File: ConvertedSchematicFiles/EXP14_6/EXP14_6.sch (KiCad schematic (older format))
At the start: 7 parts, among them U1 74393, U2 7448

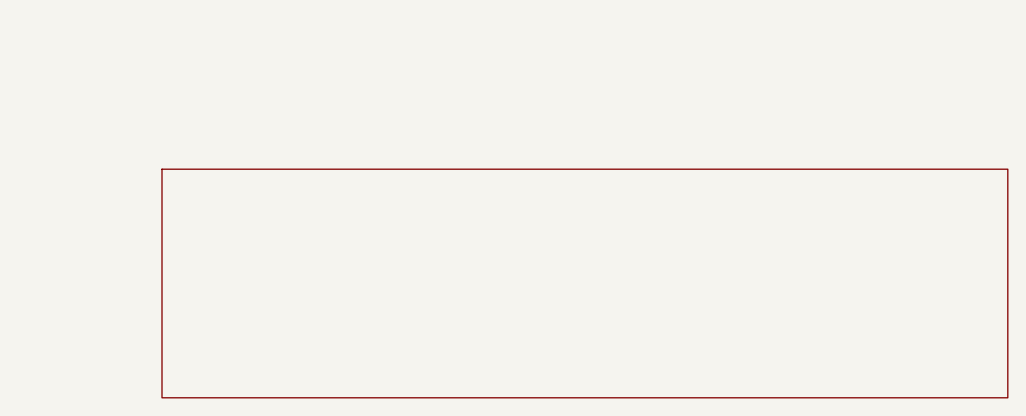
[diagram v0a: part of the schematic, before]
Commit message: Excluded some components. These no longer appear after conversion. When calling shell commands, filenames are in "quotes"
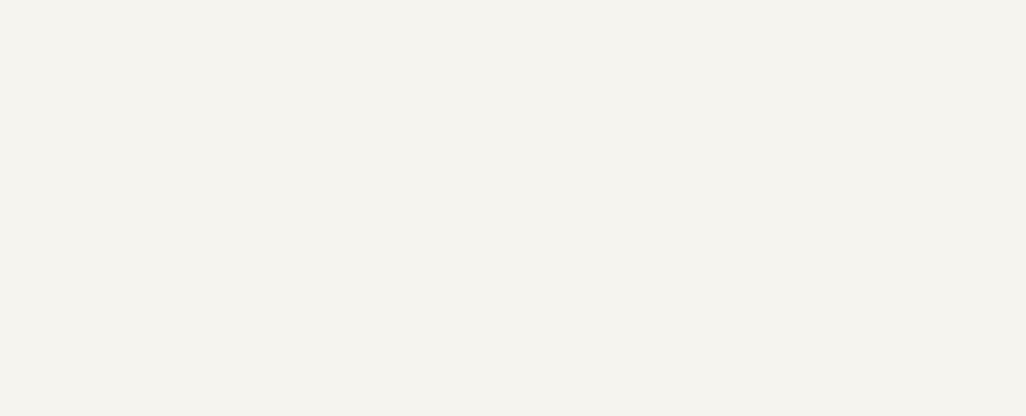
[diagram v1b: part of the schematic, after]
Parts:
- removed titleblk: titleblk, symbol TITLEBLK_PSPICE
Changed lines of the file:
@@
-	1    0    0    1
-$EndComp
-$Comp
-L TITLEBLK_PSPICE titleblk
-U 1 1 99885386
-P 9700 7200
-F 0 "titleblk" H 19400 14400 30  0001 L CNN
-F 1 "titleblk" H 19400 14480 30  0001 L CNN
-	1    9700 7200
 	1    0    0    1
 $EndComp

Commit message: Ports issue fixed. Now annotation for ports is #PWR? function added "itos"
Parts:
- removed +5V: +5V, symbol +5V_PSPICE
- removed EGND (x2): EGND, symbol EGND_PSPICE
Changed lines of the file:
@@
 $EndDescr
 $Comp
-L EGND_PSPICE EGND
+L EGND_PSPICE #PWR1
 U 1 1 14289383
 P 1400 1300
-F 0 "EGND" H 2800 2600 30  0001 L CNN
+F 0 "#PWR1" H 2800 2600 30  0001 L CNN
 F 1 "EGND" H 2800 2680 30  0001 L CNN
 	1    1400 1300
@@
 $EndComp
 $Comp
-L EGND_PSPICE EGND
+L EGND_PSPICE #PWR2
 U 1 1 46930886
 P 700 1200
-F 0 "EGND" H 1400 2400 30  0001 L CNN
+F 0 "#PWR2" H 1400 2400 30  0001 L CNN
 F 1 "EGND" H 1400 2480 30  0001 L CNN
 	1    700 1200
@@
 $EndComp
 $Comp
-L +5V_PSPICE +5V
+L +5V_PSPICE #PWR3
 U 1 1 71692777
 P 1900 600
-F 0 "+5V" H 3800 1200 30  0001 L CNN
+F 0 "#PWR3" H 3800 1200 30  0001 L CNN
 F 1 "+5V" H 3800 1280 30  0001 L CNN
 	1    1900 600

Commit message: Added LICENSE.txt
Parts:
- V1: value VPULSE -> PULSE
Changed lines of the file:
@@
 $EndDescr
 $Comp
-L EGND_PSPICE #PWR1
+L GND #PWR1
 U 1 1 14289383
 P 1400 1300
@@
 $EndComp
 $Comp
-L EGND_PSPICE #PWR2
+L GND #PWR2
 U 1 1 46930886
 P 700 1200
@@
 $EndComp
 $Comp
-L +5V_PSPICE #PWR3
+L +5V #PWR3
 U 1 1 71692777
 P 1900 600
@@
 P 700 800
 F 0 "V1" H 700 800 30  0000 L CNN
-F 1 "VPULSE" H 700 880 30  0000 L CNN
+F 1 "PULSE" H 700 880 30  0000 L CNN
 	1    700 800
 	1    0    0    1

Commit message: Orientation fix. Library components are now inverted, with +ve y axis going up. In Schematic files, +ve y axis is downwards. This is how the KiCad libraries are. As a result of the above fixed, the converted GND is now oriented correctly.
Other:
- moved on the sheet: U1, U2, V1
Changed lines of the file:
@@
 F 1 "EGND" H 2800 2680 30  0001 L CNN
 	1    1400 1300
-	1    0    0    1
+	1    0    0    -1
 $EndComp
 $Comp
@@
 F 1 "EGND" H 1400 2480 30  0001 L CNN
 	1    700 1200
-	1    0    0    1
+	1    0    0    -1
 $EndComp
 $Comp
@@
 F 1 "+5V" H 3800 1280 30  0001 L CNN
 	1    1900 600
-	1    0    0    1
+	1    0    0    -1
 $EndComp
 $Comp
@@
 F 1 "PULSE" H 700 880 30  0000 L CNN
 	1    700 800
-	1    0    0    1
+	1    0    0    -1
 $EndComp
 $Comp
@@
 F 1 "74393" H 1100 880 30  0000 L CNN
 	1    1100 800
-	1    0    0    1
+	1    0    0    -1
 $EndComp
 $Comp
@@
 F 1 "7448" H 2100 480 30  0000 L CNN
 	1    2100 400
-	1    0    0    1
+	1    0    0    -1
 $EndComp
 Wire Wire Line

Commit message: Removed the use of exec, wrote basename function, made integration with eSim easier.
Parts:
- added titleblk: titleblk, symbol titleblk_PSPICE
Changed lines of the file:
@@
-EESchema Schematic File Version 2  date Sunday 05 March 2000 04:36:24 PM IST
+EESchema Schematic File Version 2  date
 LIBS:power
 LIBS:device
@@
 LIBS:contrib
 LIBS:valves
-LIBS:ConvertedSchematicFiles/EXP14_6-cache
 EELAYER 25  0
 EELAYER END
@@
 Sheet 1 1
 Title ""
-Date "05 Mar 2000"
+Date ""
 Rev ""
 Comp ""
@@
 	1    0    0    -1
 $EndComp
+$Comp
+L titleblk_PSPICE titleblk
+U 1 1 99885386
+P 9700 7200
+F 0 "titleblk" H 19400 14400 30  0001 L CNN
+F 1 "titleblk" H 19400 14480 30  0001 L CNN
+	1    9700 7200
+	1    0    0    -1
+$EndComp
